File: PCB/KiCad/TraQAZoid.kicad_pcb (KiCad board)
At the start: 2 copper layers, 38 parts, among them SW1 MX_SW_HS, SW10 MX_SW_HS, SW11 MX_SW_HS, SW12 MX_SW_HS, SW13 MX_SW_HS, SW14 MX_SW_HS, SW15 MX_SW_HS, SW16 MX_SW_HS, SW17 MX_SW_HS, SW18 MX_SW_HS, SW19 MX_SW_HS, SW2 MX_SW_HS, SW20 MX_SW_HS, SW21 MX_SW_HS, SW22 MX_SW_HS, SW23 MX_SW_HS, SW24 MX_SW_HS, SW25 MX_SW_HS, SW26 MX_SW_HS, SW27 MX_SW_HS, SW28 MX_SW_HS, SW29 MX_SW_HS, SW3 MX_SW_HS, SW30 MX_SW_HS, SW31 MX_SW_HS, SW32 MX_SW_HS, SW33 MX_SW_HS, SW34 MX_SW_HS, SW35 MX_SW_HS, SW36 MX_SW_HS, SW37 MX_SW_HS, SW4 MX_SW_HS, SW5 MX_SW_HS, SW6 MX_SW_HS, SW7 MX_SW_HS, SW8 MX_SW_HS, SW9 MX_SW_HS, U1 tiny2040

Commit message: Sicherung
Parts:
- added D1: BAV70, Package_TO_SOT_SMD:SOT-23, B.Cu at (61.9, 56.9)
- added D10: BAV70, Package_TO_SOT_SMD:SOT-23, B.Cu at (223.8, 76.2)
- added D11: BAV70, Package_TO_SOT_SMD:SOT-23, B.Cu at (81.0, 95.2)
- added D12: BAV70, Package_TO_SOT_SMD:SOT-23, B.Cu at (119.1, 95.2)
- added D13: BAV70, Package_TO_SOT_SMD:SOT-23, B.Cu at (157.2, 95.2)
- added D14: BAV70, Package_TO_SOT_SMD:SOT-23, B.Cu at (195.3, 95.2)
- added D15: BAV70, Package_TO_SOT_SMD:SOT-23, B.Cu at (201.0, 96.2)
- added D16: BAV70, Package_TO_SOT_SMD:SOT-23, B.Cu at (99.5, 99.9)
- added D17: BAV70, Package_TO_SOT_SMD:SOT-23, B.Cu at (133.4, 100.3)
- added D18: BAV70, Package_TO_SOT_SMD:SOT-23, B.Cu at (213.2, 100.2)
- added D2: BAV70, Package_TO_SOT_SMD:SOT-23, B.Cu at (100.0, 57.1)
- added D3: BAV70, Package_TO_SOT_SMD:SOT-23, B.Cu at (135.2, 40.5)
- added D4: BAV70, Package_TO_SOT_SMD:SOT-23, B.Cu at (176.2, 57.1)
- added D5: BAV70, Package_TO_SOT_SMD:SOT-23, B.Cu at (214.3, 57.1)
- added D6: BAV70, Package_TO_SOT_SMD:SOT-23, B.Cu at (71.4, 76.2)
- added D7: BAV70, Package_TO_SOT_SMD:SOT-23, B.Cu at (109.5, 76.2)
- added D8: BAV70, Package_TO_SOT_SMD:SOT-23, B.Cu at (147.6, 76.2)
- added D9: BAV70, Package_TO_SOT_SMD:SOT-23, B.Cu at (185.7, 76.2)
- added S1: MX_stab, marbastlib:STAB_MX_P_2u, F.Cu at (128.6, 109.5)
- added S2: MX_stab, marbastlib:STAB_MX_P_7u, F.Cu at (147.6, 109.5)
- added S3: MX_stab, marbastlib:STAB_MX_P_2u, F.Cu at (166.7, 109.5)
- SW6: footprint BeiBob-KiCAD-footprints:SW_Kailh_socket_MX_optional -> BeiBob-KiCAD-footprints:SW_MX
- moved SW1 176.9 mm to (52.4, 47.6)
- moved SW14 111.2 mm to (100.0, 66.7)
- moved SW21 106.9 mm to (233.4, 66.7)
- moved SW8 96.3 mm to (185.7, 47.6)
- moved SW22 87.1 mm to (71.4, 85.7)
- moved SW4 84.6 mm to (109.5, 47.6)
- moved SW6 80.6 mm to (147.6, 47.6)
- moved SW24 80.3 mm to (109.5, 85.7)
- moved SW16 78.8 mm to (138.1, 66.7)
- moved SW28 76.5 mm to (185.7, 85.7)
- moved SW13 68.6 mm to (81.0, 66.7)
- moved SW15 64.1 mm to (119.1, 66.7)
- moved SW7 62.8 mm to (166.7, 47.6)
- moved SW29 60.1 mm to (204.8, 85.7)
- moved U1 59.0 mm to (138.7, 45.2)
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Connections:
- SW1 pad 1: unconnected-(SW1-Pad1) -> col0
- SW1 pad 2: unconnected-(SW1-Pad2) -> Net-(SW1-Pad2)
- SW10 pad 1: unconnected-(SW10-Pad1) -> Net-(D5-Pad2)
- SW10 pad 2: unconnected-(SW10-Pad2) -> col5
- SW11 pad 1: unconnected-(SW11-Pad1) -> Net-(SW11-Pad1)
- SW11 pad 2: unconnected-(SW11-Pad2) -> col5
- SW12 pad 1: unconnected-(SW12-Pad1) -> col0
- SW12 pad 2: unconnected-(SW12-Pad2) -> Net-(D6-Pad1)
- SW13 pad 1: unconnected-(SW13-Pad1) -> Net-(D6-Pad2)
- SW13 pad 2: unconnected-(SW13-Pad2) -> col1
- SW14 pad 1: unconnected-(SW14-Pad1) -> col0
- SW14 pad 2: unconnected-(SW14-Pad2) -> Net-(D7-Pad1)
- SW15 pad 1: unconnected-(SW15-Pad1) -> Net-(D7-Pad2)
- SW15 pad 2: unconnected-(SW15-Pad2) -> col1
- SW16 pad 1: unconnected-(SW16-Pad1) -> col2
- SW16 pad 2: unconnected-(SW16-Pad2) -> Net-(D8-Pad1)
- SW17 pad 1: unconnected-(SW17-Pad1) -> Net-(D8-Pad2)
- SW17 pad 2: unconnected-(SW17-Pad2) -> col3
- SW18 pad 1: unconnected-(SW18-Pad1) -> col2
- SW18 pad 2: unconnected-(SW18-Pad2) -> Net-(D9-Pad1)
- SW19 pad 1: unconnected-(SW19-Pad1) -> Net-(D9-Pad2)
- SW19 pad 2: unconnected-(SW19-Pad2) -> col3
- SW2 pad 1: unconnected-(SW2-Pad1) -> Net-(SW2-Pad1)
- SW2 pad 2: unconnected-(SW2-Pad2) -> col1
- SW20 pad 1: unconnected-(SW20-Pad1) -> col4
- SW20 pad 2: unconnected-(SW20-Pad2) -> Net-(D10-Pad1)
- SW21 pad 1: unconnected-(SW21-Pad1) -> Net-(D10-Pad2)
- SW21 pad 2: unconnected-(SW21-Pad2) -> col5
- SW22 pad 1: unconnected-(SW22-Pad1) -> col0
- SW22 pad 2: unconnected-(SW22-Pad2) -> Net-(D11-Pad1)
- SW23 pad 1: unconnected-(SW23-Pad1) -> Net-(D11-Pad2)
- SW23 pad 2: unconnected-(SW23-Pad2) -> col1
- SW24 pad 1: unconnected-(SW24-Pad1) -> col0
- SW24 pad 2: unconnected-(SW24-Pad2) -> Net-(D12-Pad1)
- SW25 pad 1: unconnected-(SW25-Pad1) -> Net-(D12-Pad2)
- SW25 pad 2: unconnected-(SW25-Pad2) -> col1
- SW26 pad 1: unconnected-(SW26-Pad1) -> col2
- SW26 pad 2: unconnected-(SW26-Pad2) -> Net-(D13-Pad1)
- SW27 pad 1: unconnected-(SW27-Pad1) -> Net-(D13-Pad2)
- SW27 pad 2: unconnected-(SW27-Pad2) -> col3
- SW28 pad 1: unconnected-(SW28-Pad1) -> col2
- SW28 pad 2: unconnected-(SW28-Pad2) -> Net-(D14-Pad1)
- SW29 pad 1: unconnected-(SW29-Pad1) -> Net-(D14-Pad2)
- SW29 pad 2: unconnected-(SW29-Pad2) -> col3
- SW3 pad 1: unconnected-(SW3-Pad1) -> col0
- SW3 pad 2: unconnected-(SW3-Pad2) -> Net-(D2-Pad1)
- SW30 pad 1: unconnected-(SW30-Pad1) -> col4
- SW30 pad 2: unconnected-(SW30-Pad2) -> Net-(SW30-Pad2)
- SW31 pad 1: unconnected-(SW31-Pad1) -> col4
- SW31 pad 2: unconnected-(SW31-Pad2) -> Net-(SW31-Pad2)
- SW32 pad 1: unconnected-(SW32-Pad1) -> Net-(SW32-Pad1)
- SW32 pad 2: unconnected-(SW32-Pad2) -> col5
- SW33 pad 1: unconnected-(SW33-Pad1) -> col4
- SW33 pad 2: unconnected-(SW33-Pad2) -> Net-(SW33-Pad2)
- SW34 pad 1: unconnected-(SW34-Pad1) -> Net-(SW37-Pad1)
- SW34 pad 2: unconnected-(SW34-Pad2) -> col5
- SW35 pad 1: unconnected-(SW35-Pad1) -> col4
- SW35 pad 2: unconnected-(SW35-Pad2) -> Net-(SW35-Pad2)
- SW36 pad 1: unconnected-(SW36-Pad1) -> Net-(SW36-Pad1)
- SW36 pad 2: unconnected-(SW36-Pad2) -> col5
- SW37 pad 1: unconnected-(SW37-Pad1) -> Net-(SW37-Pad1)
- SW37 pad 2: unconnected-(SW37-Pad2) -> col5
- SW4 pad 1: unconnected-(SW4-Pad1) -> Net-(D2-Pad2)
- SW4 pad 2: unconnected-(SW4-Pad2) -> col1
- SW5 pad 1: unconnected-(SW5-Pad1) -> col2
- SW5 pad 2: unconnected-(SW5-Pad2) -> Net-(D3-Pad1)
- SW6 pad 1: unconnected-(SW6-Pad1) -> Net-(D3-Pad2)
- SW6 pad 2: unconnected-(SW6-Pad2) -> col3
- SW7 pad 1: unconnected-(SW7-Pad1) -> col2
- SW7 pad 2: unconnected-(SW7-Pad2) -> Net-(D4-Pad1)
- SW8 pad 1: unconnected-(SW8-Pad1) -> Net-(D4-Pad2)
- SW8 pad 2: unconnected-(SW8-Pad2) -> col3
- SW9 pad 1: unconnected-(SW9-Pad1) -> col4
- SW9 pad 2: unconnected-(SW9-Pad2) -> Net-(D5-Pad1)
- U1 pad 10: unconnected-(U1-Pad10) -> col3
- U1 pad 11: unconnected-(U1-Pad11) -> row2
- U1 pad 12: unconnected-(U1-Pad12) -> row3
- U1 pad 13: unconnected-(U1-Pad13) -> row4
- U1 pad 14: unconnected-(U1-Pad14) -> row5
- U1 pad 15: unconnected-(U1-Pad15) -> col4
- U1 pad 16: unconnected-(U1-Pad16) -> col5
- U1 pad 4: unconnected-(U1-Pad4) -> col0
- U1 pad 5: unconnected-(U1-Pad5) -> col1
- U1 pad 6: unconnected-(U1-Pad6) -> row0
- U1 pad 7: unconnected-(U1-Pad7) -> row1
- U1 pad 9: unconnected-(U1-Pad9) -> col2
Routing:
- net col5: track 0.00 -> 347.4 mm
- net row1: track 0.00 -> 223.7 mm, vias 0 -> 1
- net col4: track 0.00 -> 223.5 mm
- net row3: track 0.00 -> 218.3 mm
- net row0: track 0.00 -> 177.7 mm
- net row2: track 0.00 -> 154.7 mm
- net row4: track 0.00 -> 122.4 mm
- net col1: track 0.00 -> 115.1 mm
- net row5: track 0.00 -> 96.9 mm
- net col0: track 0.00 -> 89.6 mm
- net col3: track 0.00 -> 88.4 mm
- net Net-(SW30-Pad2): track 0.00 -> 44.3 mm
- net col2: track 0.00 -> 43.1 mm
- net Net-(SW37-Pad1): track 0.00 -> 42.1 mm
- net Net-(SW31-Pad2): track 0.00 -> 25.1 mm
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
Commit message: Fertig?
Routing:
- net col0: track 89.6 -> 257.3 mm
- net col2: track 43.1 -> 195.5 mm
- net col3: track 88.4 -> 212.2 mm
- net col1: track 115.1 -> 230.4 mm
- net col4: track 223.5 -> 316.2 mm
- net Net-(SW11-Pad1): track 8.65 -> 78.6 mm, vias 0 -> 1
- net row5: track 96.9 -> 151.9 mm, vias 0 -> 1
- net row4: track 122.4 -> 175.3 mm, vias 0 -> 1
- net row0: track 177.7 -> 225.8 mm
- net row1: track 223.7 -> 190.7 mm, vias 1 -> 0
- net row2: track 154.7 -> 184.3 mm, vias 0 -> 1
- net Net-(D12-Pad1): track 0.00 -> 15.9 mm
- net Net-(D8-Pad1): track 0.00 -> 15.9 mm
- net Net-(D13-Pad1): track 0.00 -> 15.9 mm
- net Net-(D13-Pad2): track 0.00 -> 13.9 mm
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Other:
- board outline added: 212 x 85 mm
- board text added: "TraQAZoid v2"
- board text added: "https://github.com/Technofrikus/TraQAZoid"

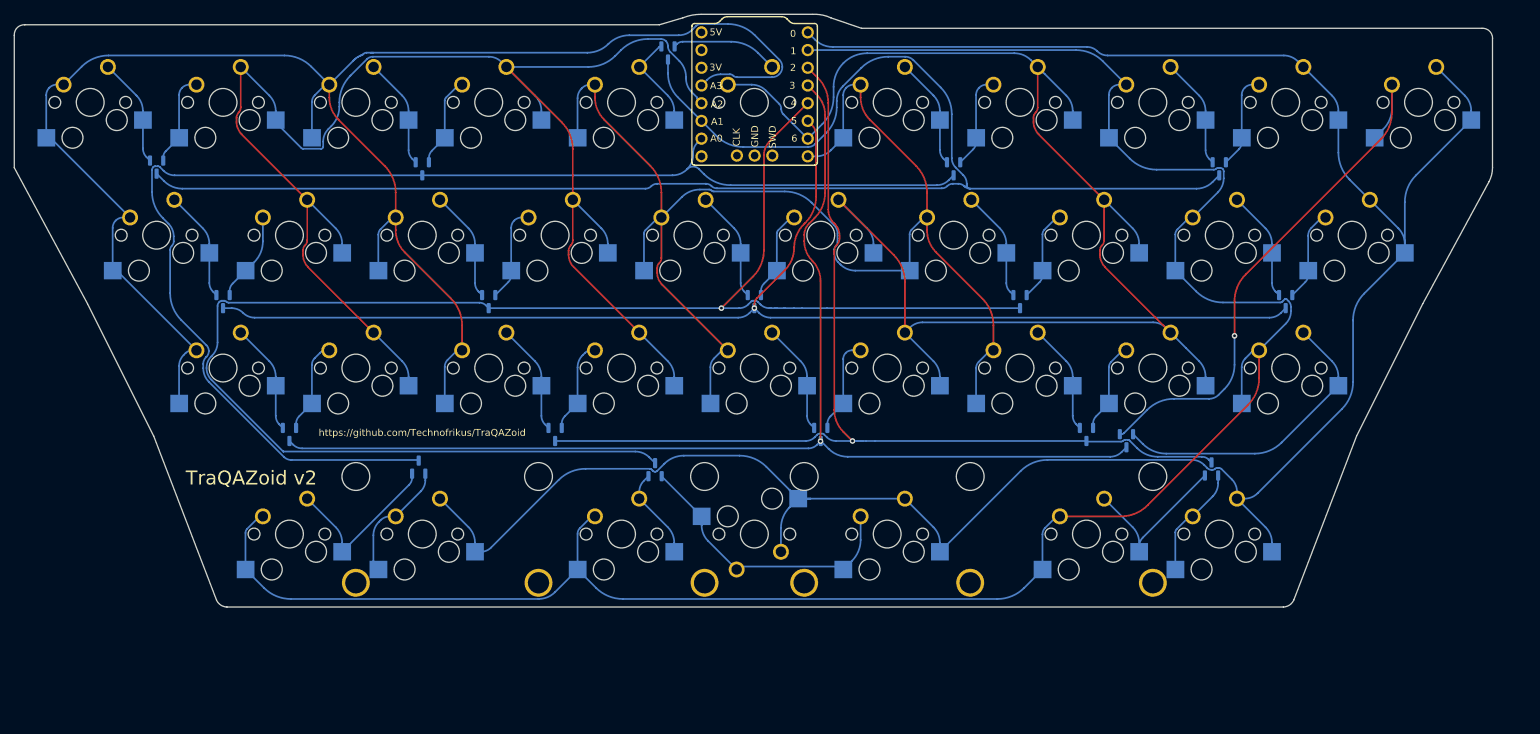
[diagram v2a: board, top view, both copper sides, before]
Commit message: PCB kleiner gemacht.
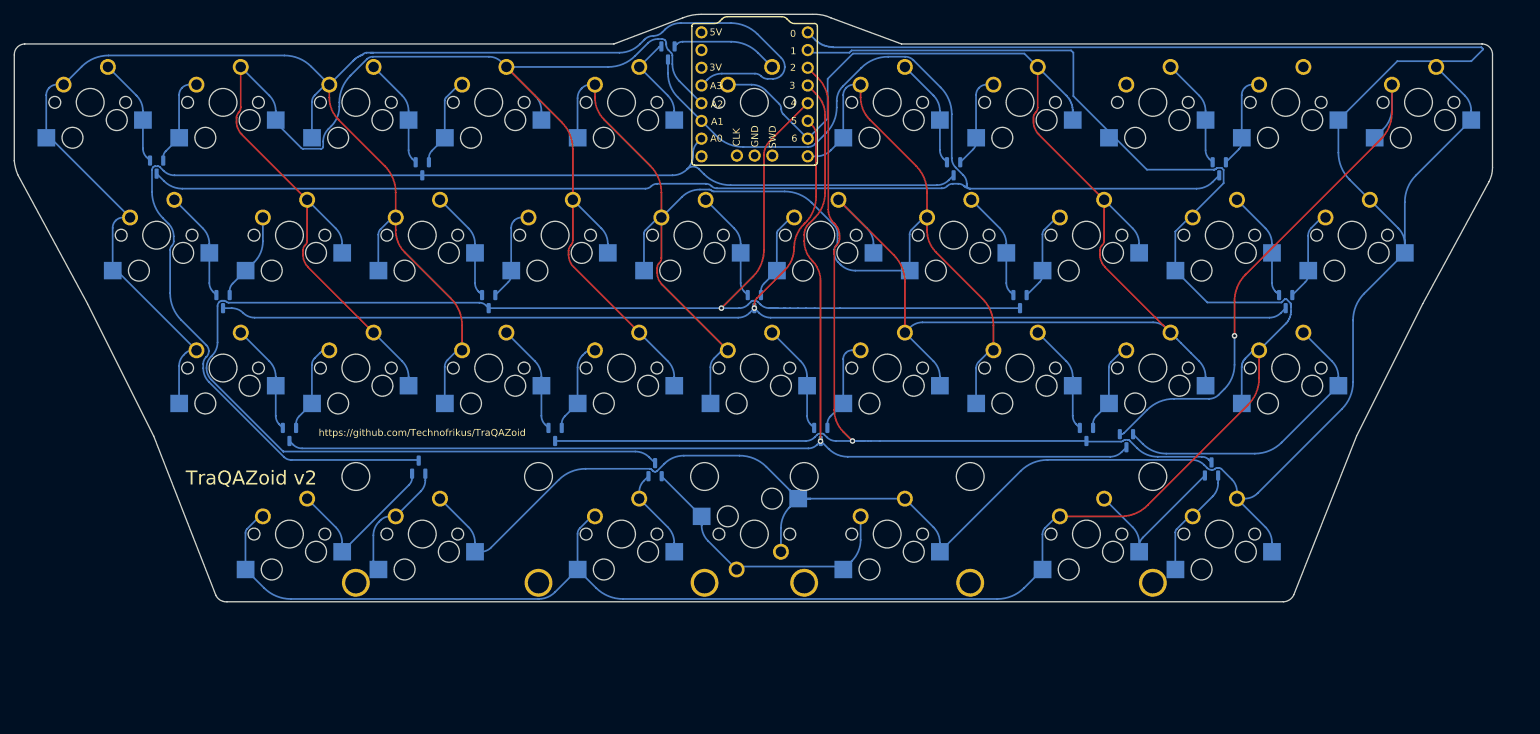
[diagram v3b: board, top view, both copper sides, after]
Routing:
- net col5: track 345.5 -> 386.0 mm
- net col4: track 316.2 -> 313.1 mm
- net col1: track 230.4 -> 231.8 mm
- net col0: track 257.3 -> 258.5 mm
- net col3: track 212.2 -> 213.0 mm
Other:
- board size 212 x 85 mm -> 212 x 84.3 mm
